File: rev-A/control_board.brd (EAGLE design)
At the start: 112.4 x 69.8 mm, 126 parts, among them IC1 W5500, IC3 ATMEGA32U4-AU, J1 USB_B_PTH, K1 G5V1, K2 G5V1, K3 G5V1, SW1 SPST_TACT-KMR2, Y1 8MHz, Y2 25MHz, 10pF

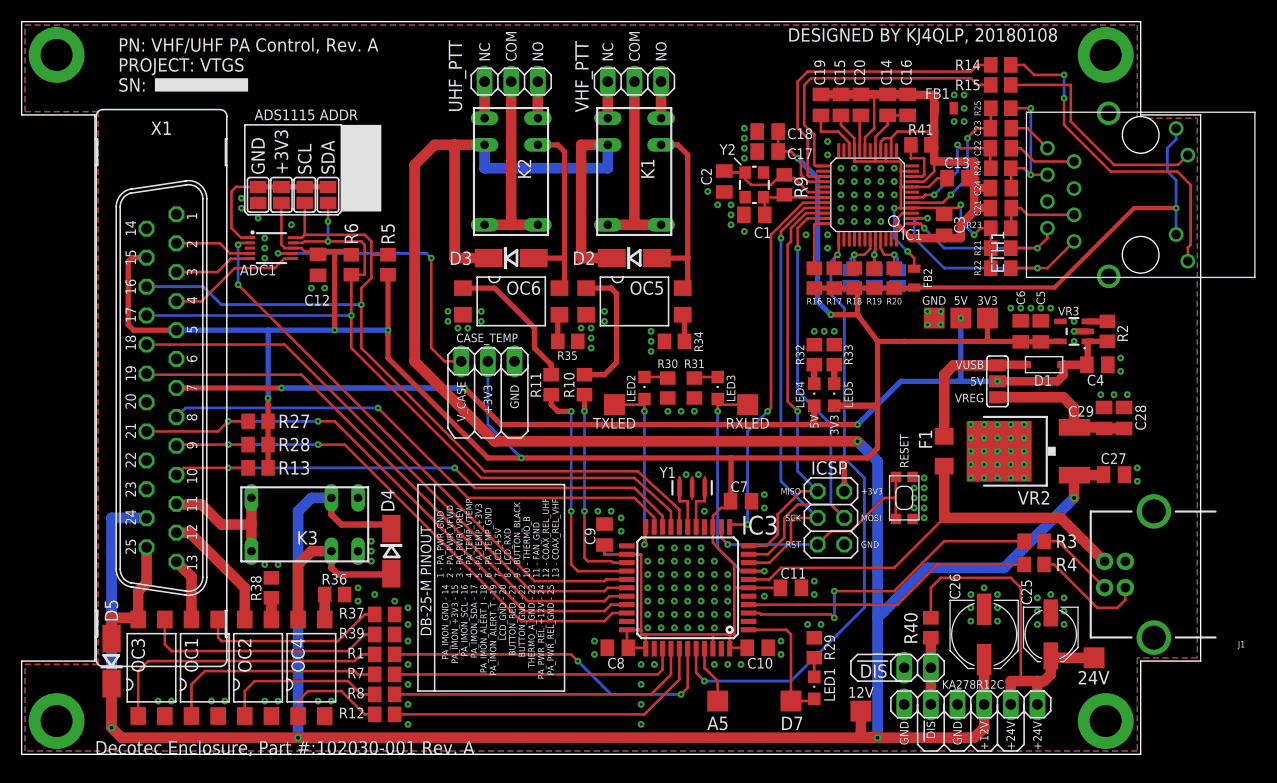
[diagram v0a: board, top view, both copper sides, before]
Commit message: lots of updates, added caps for ADC, swapped out 5v vreg, moved a lot of parts around, added flyback diodes to relays.
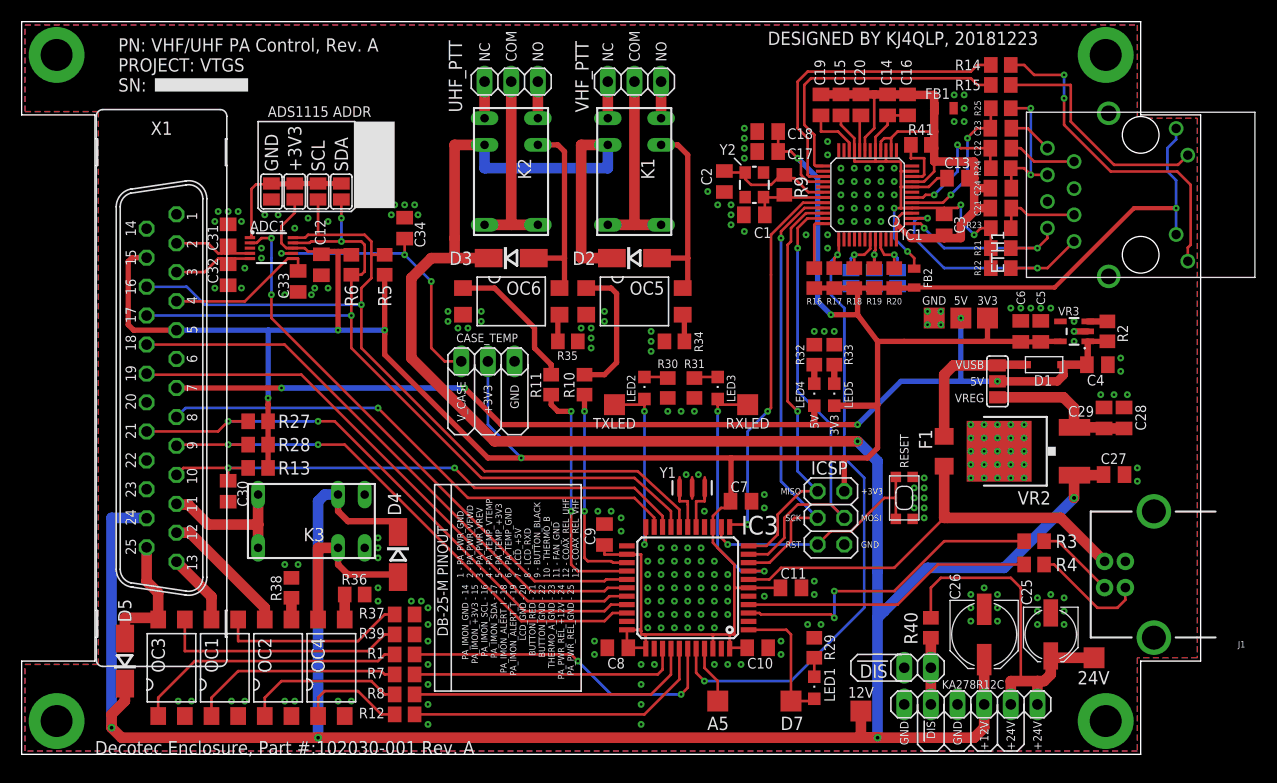
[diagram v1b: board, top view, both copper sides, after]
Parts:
- added C30, C31, C32, C33, C34: .1uF, rcl:C0805K
- moved OC1 1.91 mm to (19.4, 8.26)
- moved OC2 1.91 mm to (24.4, 8.26)
- moved OC4 1.91 mm to (29.5, 8.26)
- moved R1 1.91 mm to (36.5, 9.53)
- moved R12 1.91 mm to (36.5, 3.81)
- moved R36 1.91 mm to (31.8, 15.2)
- moved R37 1.91 mm to (36.5, 13.3)
- moved R38 1.91 mm to (25.7, 15.9)
- moved R39 1.91 mm to (36.5, 11.4)
- moved R7 1.91 mm to (36.5, 7.62)
- moved R8 1.91 mm to (36.5, 5.71)
- moved OC3 1.90 mm to (14.3, 8.26)
- moved SJ1 1.31 mm to (28.3, 53.7)
- moved SJ2 1.31 mm to (30.5, 53.7)
- moved SJ3 1.31 mm to (26.0, 53.7)
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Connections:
- net 0_RX_THERMO: now also C30.1
- net GND: now also C30.2, C31.2, C32.2, C33.2, C34.2
- net V_CASE: now also C34.1
- net V_FWD: now also C31.1
- net V_REV: now also C32.1
- net V_TEMP: now also C33.1
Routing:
- net +12V: track 331.1 -> 321.3 mm
- net A3_PA_PWR_REL: track 33.5 -> 31.6 mm
- net A2_PA_FAN: track 31.5 -> 29.6 mm
- net A1_UHF_COAX_REL: track 29.6 -> 27.7 mm
- net A0_VHF_COAX_REL: track 27.7 -> 25.8 mm
- net V_TEMP: track 12.8 -> 14.5 mm
- net ADDR: track 15.0 -> 13.5 mm
- net N$1: track 27.5 -> 26.0 mm
- net 0_RX_THERMO: track 51.5 -> 52.7 mm
- net VHF_COAX_REL: track 6.10 -> 6.89 mm
- net UHF_COAX_REL: track 11.7 -> 12.5 mm
- net V_FWD: track 7.40 -> 8.17 mm
- net PA_PWR_REL: track 11.8 -> 12.6 mm
- net N$12: track 21.1 -> 20.4 mm
- net FAN: track 13.0 -> 13.7 mm
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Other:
- board text added: "DESIGNED BY KJ4QLP, 20181223"
- board text removed: "DESIGNED BY KJ4QLP, 20180108"

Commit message: added to silkscreen, added osh park top/bottom pngs.  This version ordered.
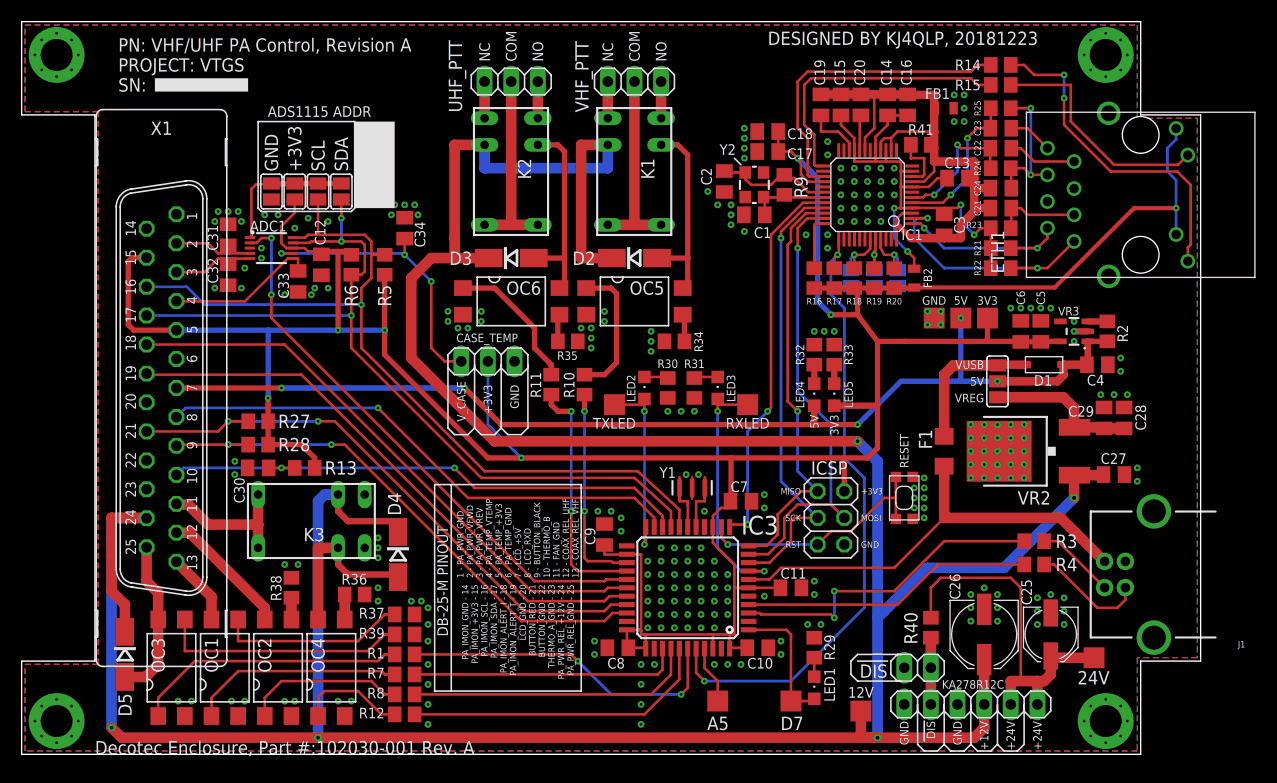
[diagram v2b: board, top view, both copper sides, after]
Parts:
- moved R13 4.45 mm to (27.0, 27.3)
- moved C30 3.62 mm to (22.5, 27.3), turned to 180 degrees
- moved D5 0.63 mm to (9.84, 9.53), turned to 270 degrees
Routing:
- net +12V: track 321.3 -> 331.3 mm
- net +3V3: track 309.4 -> 312.6 mm
- net PA_PWR_REL: track 12.6 -> 15.5 mm
- net 0_RX_THERMO: track 52.7 -> 52.1 mm
- net GND: vias 248 -> 258
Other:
- board text added: "1 2 3 4 5 6 7 8 9 10 11 12 13"
- board text added: "14 15 16 17 18 19 20 21 22 23 24 25"
- board text added: "PN: VHF/UHF PA Control, Revision A"
- board text removed: "PN: VHF/UHF PA Control, Rev. A"

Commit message: fixed R41 value to 12.4k
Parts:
- R41: value 49.9 -> 12.4k
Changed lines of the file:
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@@
 <attribute name="VALUE" x="48.26" y="40.64" size="1.27" layer="27" rot="R180"/>
 </element>
-<element name="R41" library="rcl" library_urn="urn:adsk.eagle:library:334" package="R0805" package3d_urn="urn:adsk.eagle:package:23553/2" value="49.9" x="85.725" y="58.1025" smashed="yes" rot="R180">
+<element name="R41" library="rcl" library_urn="urn:adsk.eagle:library:334" package="R0805" package3d_urn="urn:adsk.eagle:package:23553/2" value="12.4k" x="85.725" y="58.1025" smashed="yes" rot="R180">
 <attribute name="NAME" x="85.725" y="59.055" size="1.016" layer="25" rot="R180" align="top-center"/>
 <attribute name="SPICEPREFIX" value="R" x="85.725" y="58.1025" size="1.778" layer="27" rot="R180" display="off"/>
